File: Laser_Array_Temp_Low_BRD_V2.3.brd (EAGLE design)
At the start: 123 x 160.1 mm, 143 parts, among them J1 LASER_MOD, J10 LASER_MOD, J11 LASER_MOD, J12 LASER_MOD, J13 22-23-2021, J14 22-23-2021, J15 22-23-2021, J16 22-23-2021, J17 22-23-2021, J18 22-23-2021, J19 22-23-2021, J2 LASER_MOD, J20 22-23-2021, J21 22-23-2021, J22 22-23-2021, J23 22-23-2021, J24 22-23-2021, J3 LASER_MOD, J4 LASER_MOD, J5 LASER_MOD, J6 LASER_MOD, J7 LASER_MOD, J8 LASER_MOD, J9 LASER_MOD, U1 TCA9546A, U2 TCA9546A, U3 TCA9546A, X1 22-23-2041, X10 22-23-2041, X11 22-23-2041, X12 22-23-2041, X13 22-23-2041, X14 22-23-2041, X2 22-23-2041, X3 22-23-2041, X4 22-23-2041, X5 22-23-2041, X6 22-23-2041, X7 22-23-2041, X8 22-23-2041, X9 22-23-2041

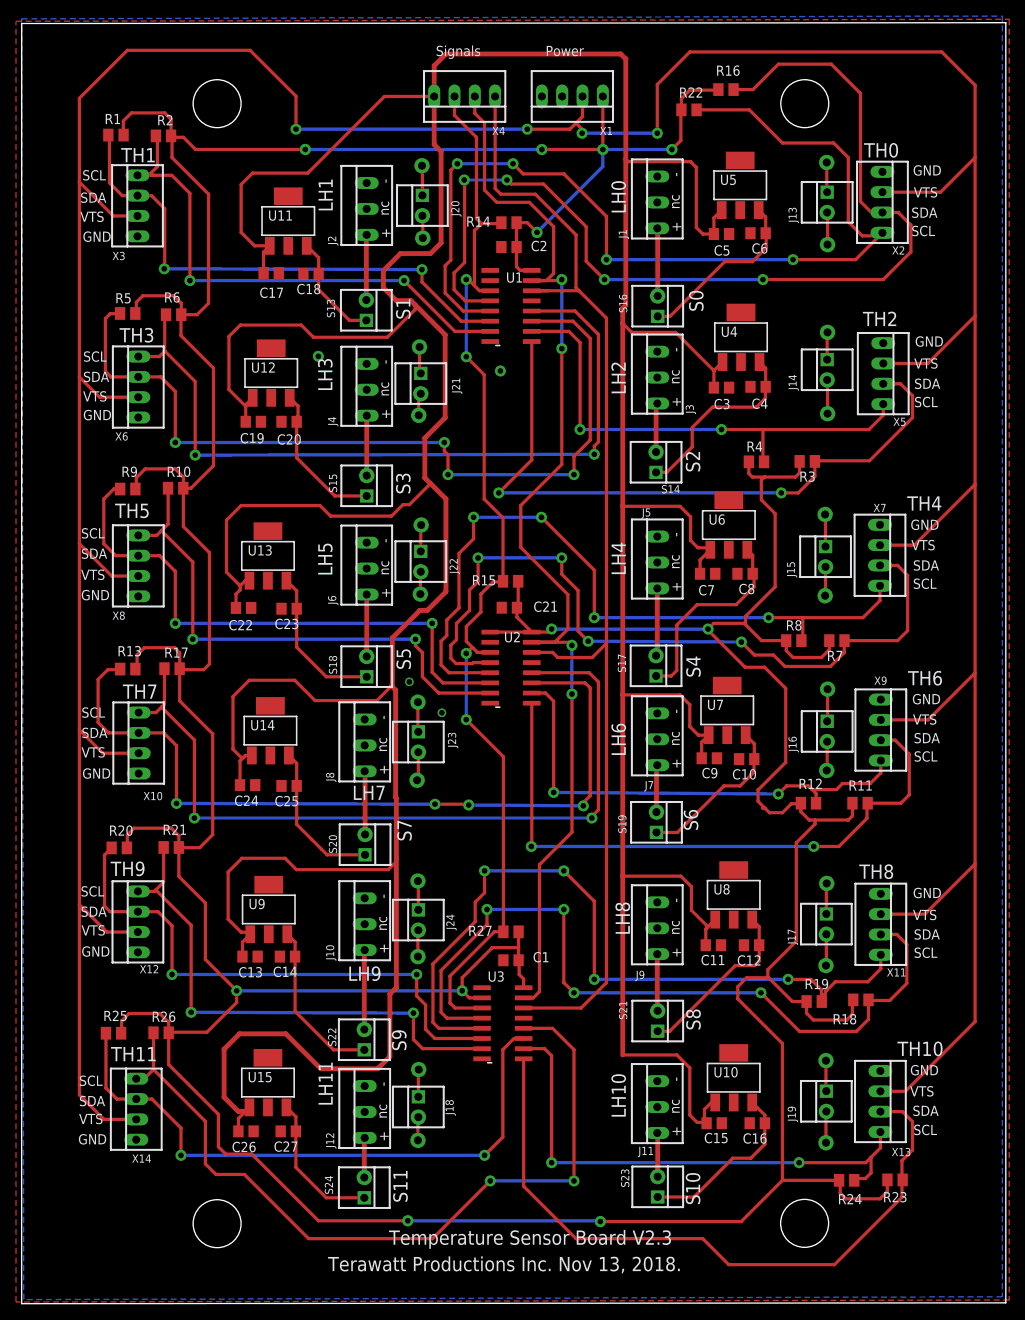
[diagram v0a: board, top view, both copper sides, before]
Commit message: Finished Laser_Array next versions, all three boards including revised charger board
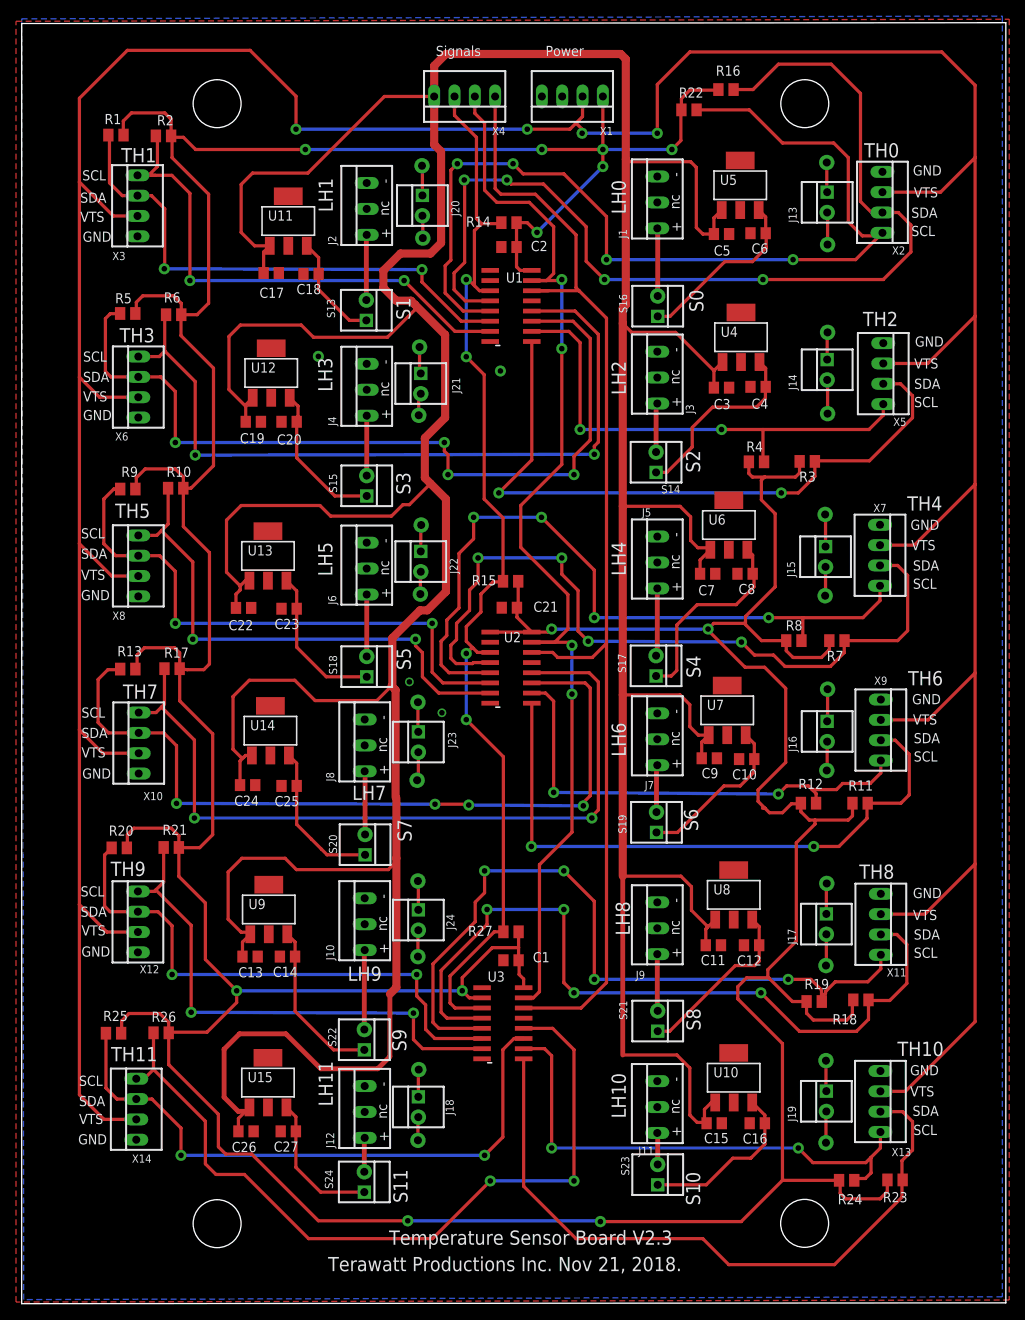
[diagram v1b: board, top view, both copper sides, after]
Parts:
- moved S23 1.52 mm to (65.1, 16.1)
- moved S24 0.71 mm to (28.4, 15.2)
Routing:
- net N$10: track 5.48 -> 3.96 mm
- net SC10: track 65.5 -> 64.4 mm
- net N$12: track 4.97 -> 4.26 mm
- net N$49: track 22.0 -> 21.4 mm
- net VDD: vias 11 -> 12
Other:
- board text added: "Terawatt Productions Inc. Nov 21, 2018."
- board text removed: "Terawatt Productions Inc. Nov 13, 2018."
